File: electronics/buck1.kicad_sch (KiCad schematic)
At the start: 14 parts, among them U2 TPS54302DDCR

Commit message: Integrate onboard RP2040 and drawing-based EV3 jacks on A1 PCB
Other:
- title: Quadcuber A0 / buck1 / ENGINEERING HOLD -> Quadcuber A1 / buck1 / ENGINEERING HOLD

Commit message: Correct audited power BOM and add bounded VM discharge protection
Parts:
- C20: MPN GRM32ER71E106KA12L -> GRM32DR71E106KA12L
- C25: MPN GRM1885C1H750JA01D -> C0603C750J5GACTU; Manufacturer Murata -> KEMET

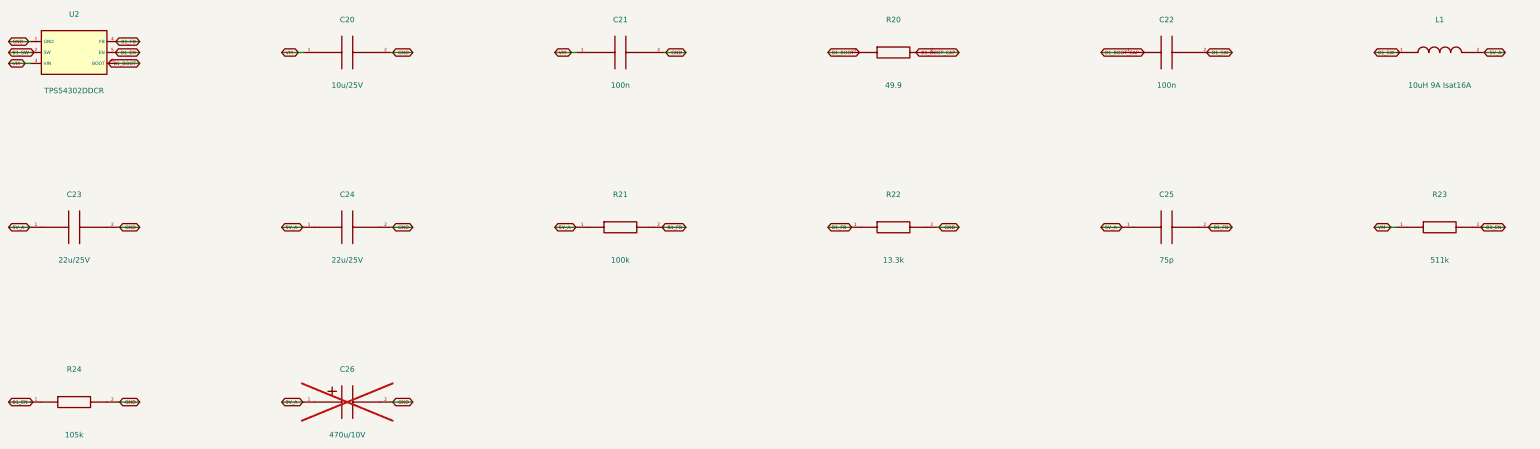
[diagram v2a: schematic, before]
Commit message: Migrate A1 to KiCad 10 and record blocked vendor-model transients
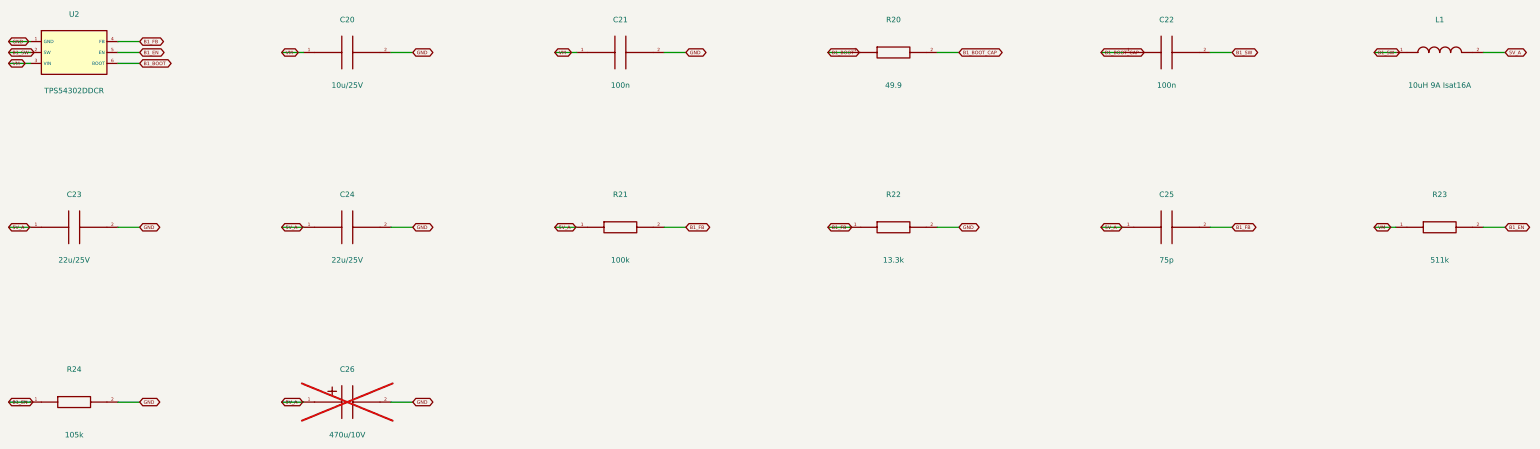
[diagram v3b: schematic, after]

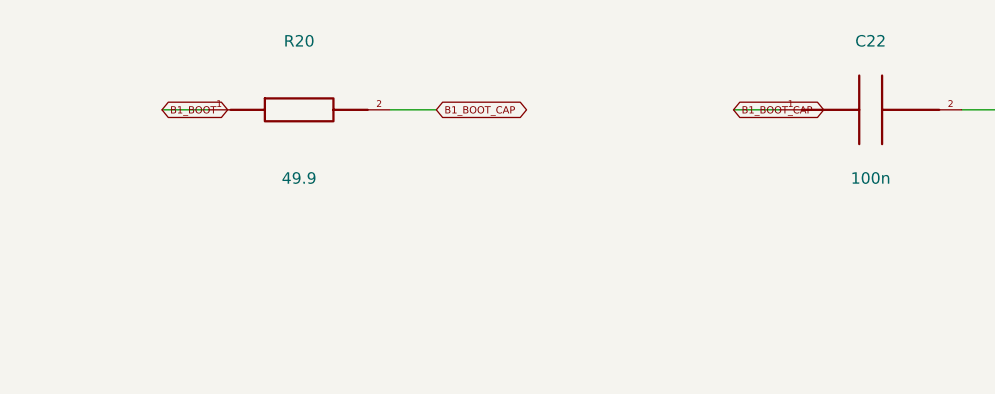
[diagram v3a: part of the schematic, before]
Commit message: Correct A1 bootstrap routing and precision feedback with verified artifacts
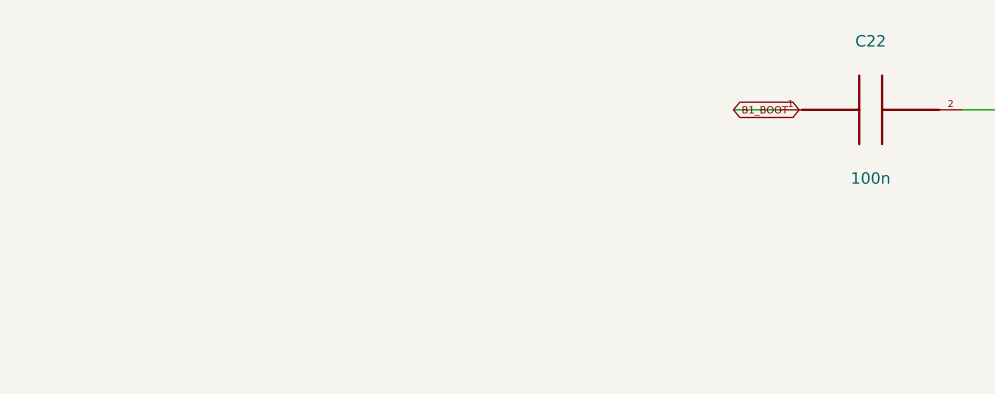
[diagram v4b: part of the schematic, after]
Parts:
- removed R20: 49.9, Quadcuber:R_0603_1608Metric, symbol Quadcuber:R20
- R21: MPN RC0603FR-07100KL -> RT0603BRD07100KL
- R22: MPN RC0603FR-0713K3L -> RT0603BRD0713K3L
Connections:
- net B1_BOOT_CAP is gone; now on net B1_BOOT: C22.1
